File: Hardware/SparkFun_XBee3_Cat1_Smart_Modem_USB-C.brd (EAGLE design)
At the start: 53.3 x 59.7 mm, 112 parts, among them J1 USB Female Type C Connector, J3 USB Female Type C Connector, J4 QWIIC_RIGHT_ANGLE, U1 FSUSB30MUX_MSOP10, U2 AP63203, U3 ESD Diode, U5 ESD Diode, U6 CP210X

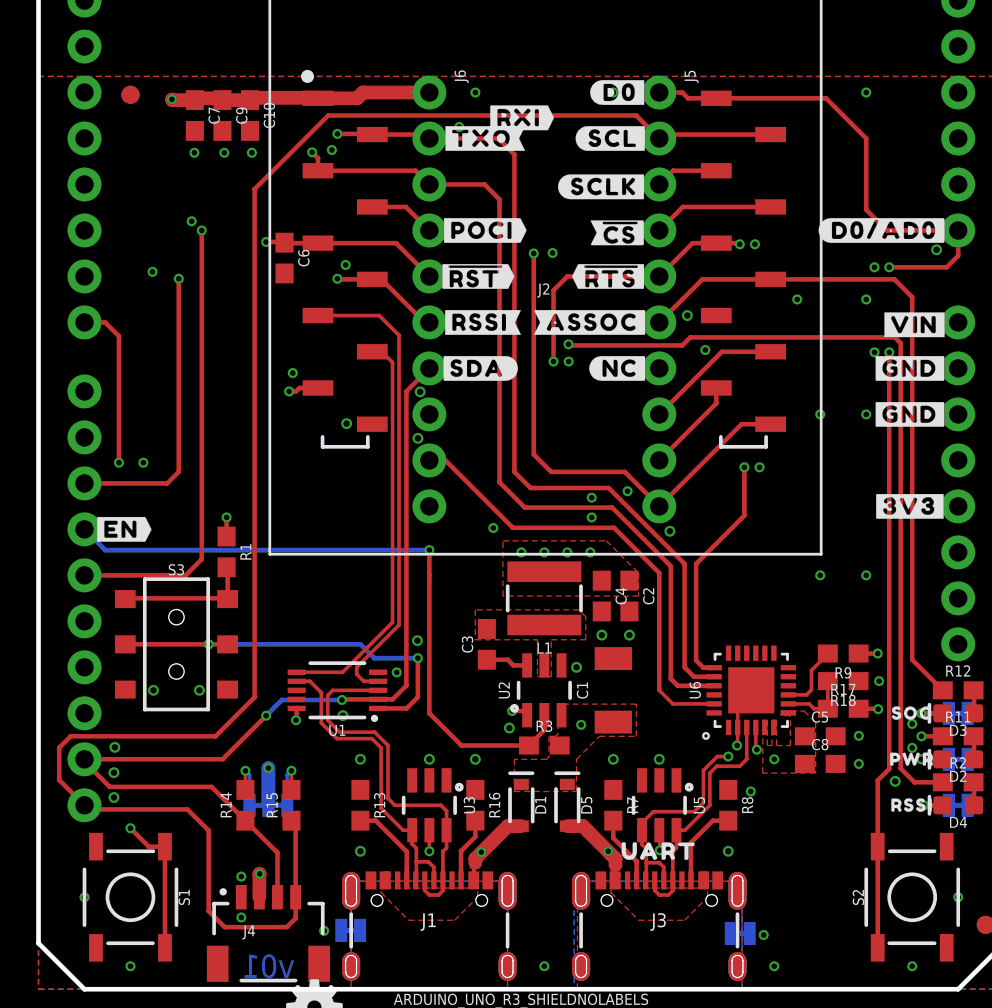
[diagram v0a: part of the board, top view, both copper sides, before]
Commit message: Updates many traces
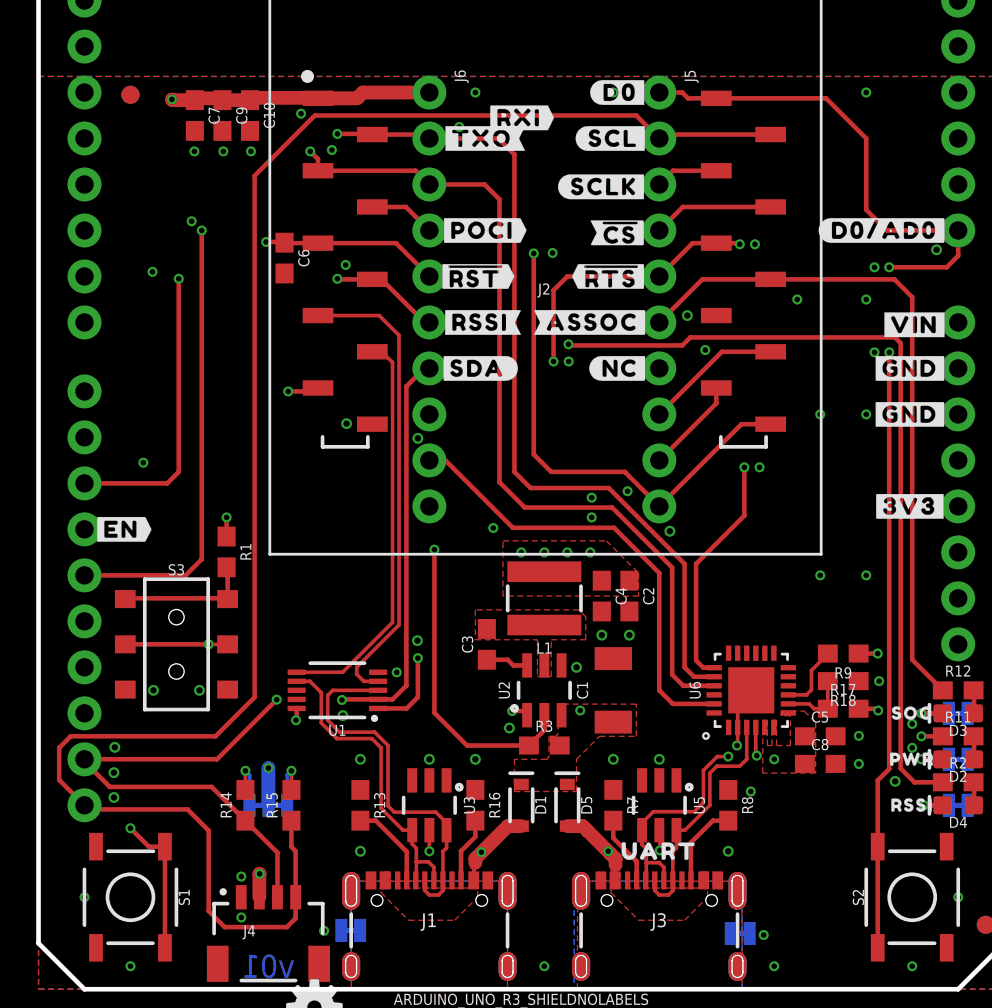
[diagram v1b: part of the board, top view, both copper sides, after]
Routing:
- net D7/!CTS!: track 49.5 -> 45.2 mm, vias 1 -> 0
- net D2/SPI_CLK: track 38.5 -> 37.3 mm
- net GND: vias 73 -> 72

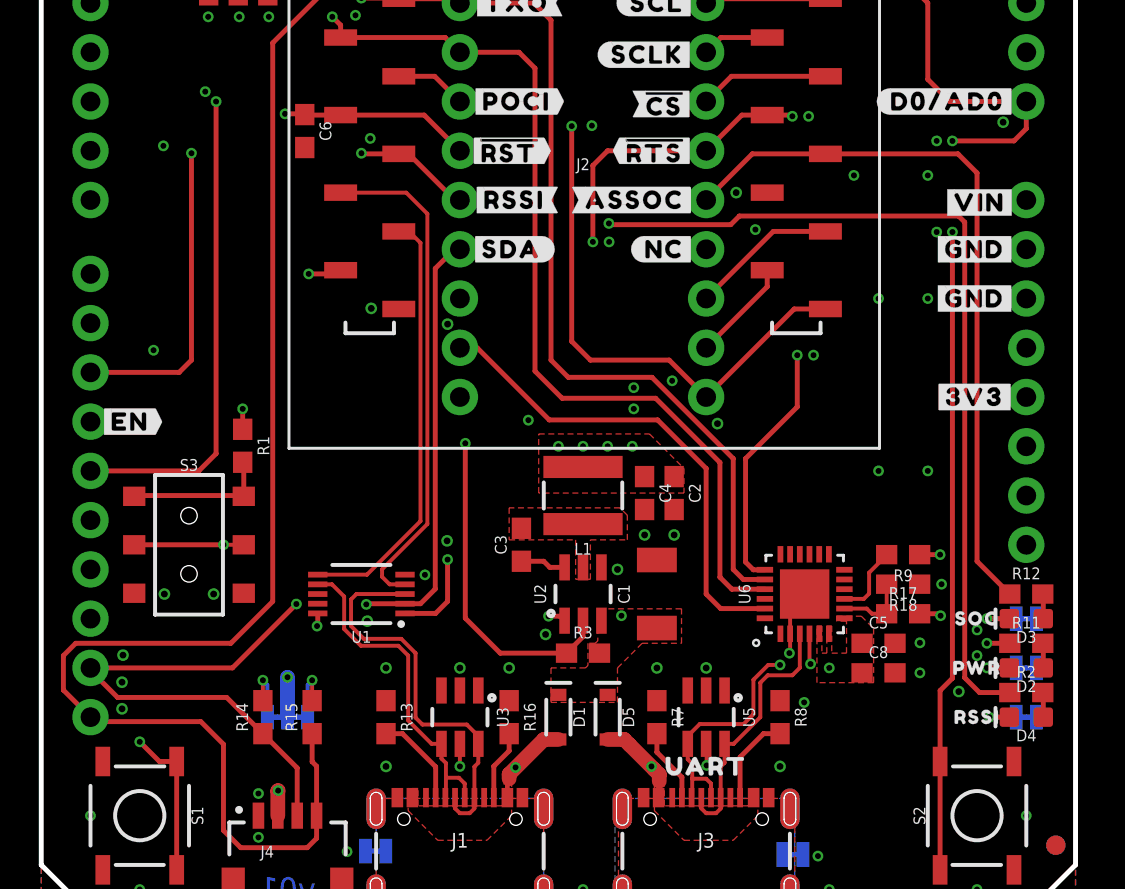
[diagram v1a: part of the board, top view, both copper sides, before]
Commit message: Makes all drill sizes uniform (0.012")
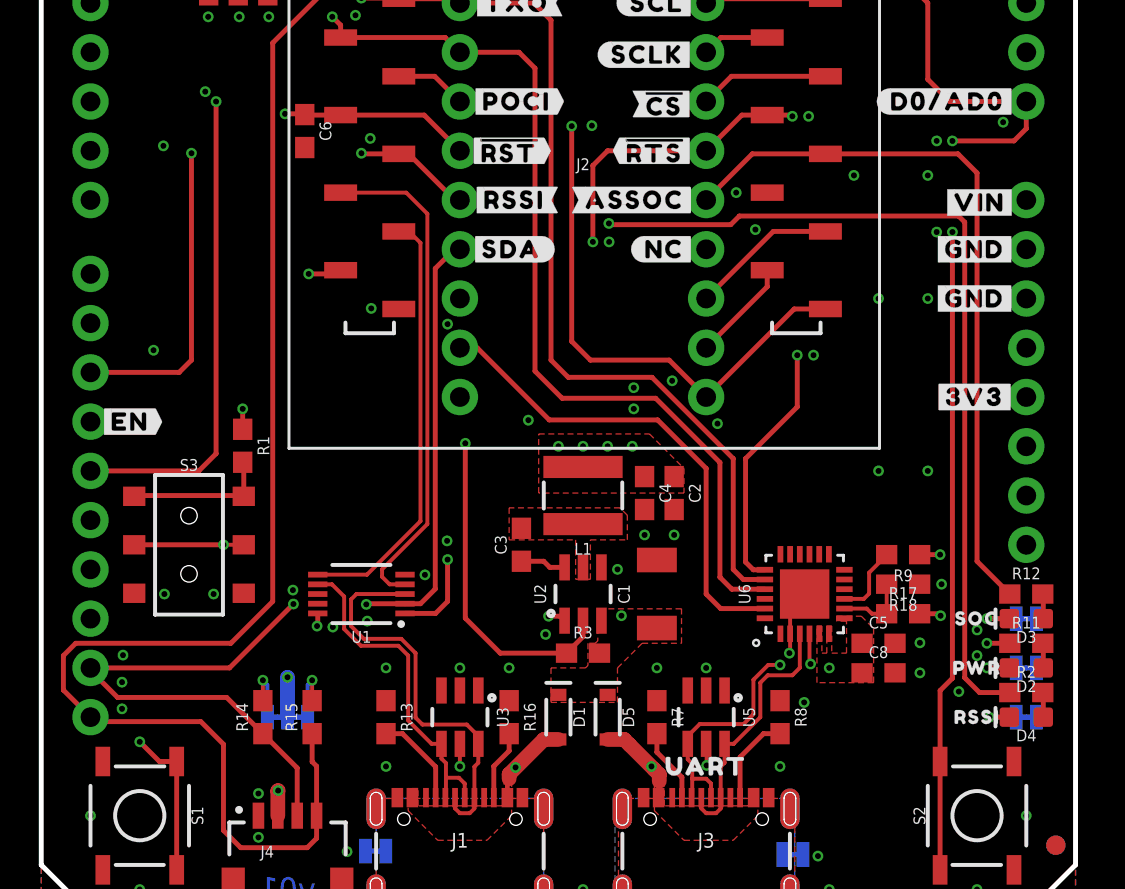
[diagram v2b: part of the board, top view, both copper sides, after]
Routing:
- net GND: vias 72 -> 74
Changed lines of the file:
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@@
 <wire x1="16.7974" y1="16.01" x2="16.764" y2="15.9766" width="0.254" layer="1"/>
 <via x="16.764" y="15.9766" extent="1-16" drill="0.3048"/>
-<wire x1="16.764" y1="15.9766" x2="13.1756" y2="15.9766" width="0.254" layer="2"/>
-<wire x1="13.1756" y1="15.9766" x2="13.1572" y2="15.995" width="0.254" layer="2"/>
-<via x="13.1572" y="15.995" extent="1-16" drill="0.3048"/>
+<wire x1="16.764" y1="15.9766" x2="13.0232" y2="15.9766" width="0.254" layer="2"/>
+<wire x1="13.0232" y1="15.9766" x2="13.0048" y2="15.995" width="0.254" layer="2"/>
+<via x="13.0048" y="15.995" extent="1-16" drill="0.3048"/>
 <wire x1="13.2" y1="5.08" x2="13.2" y2="7.54" width="0.254" layer="1"/>
 <wire x1="13.2" y1="7.54" x2="11.43" y2="9.31" width="0.254" layer="1"/>
@@
 <wire x1="3.937" y1="11.176" x2="2.54" y2="12.573" width="0.254" layer="1"/>
 <wire x1="2.54" y1="12.573" x2="2.54" y2="12.7" width="0.254" layer="1"/>
-<wire x1="2.54" y1="12.7" x2="9.8622" y2="12.7" width="0.254" layer="1"/>
-<wire x1="9.8622" y1="12.7" x2="13.1572" y2="15.995" width="0.254" layer="1"/>
+<wire x1="2.54" y1="12.7" x2="9.7098" y2="12.7" width="0.254" layer="1"/>
+<wire x1="9.7098" y1="12.7" x2="13.0048" y2="15.995" width="0.254" layer="1"/>
 <wire x1="20.32" y1="33.2994" x2="20.32" y2="16.77086875" width="0.254" layer="1"/>
 <wire x1="21.3106" y1="34.29" x2="20.32" y2="33.2994" width="0.254" layer="1"/>
@@
 <contactref element="RLED" pad="1"/>
 <contactref element="J6" pad="10"/>
-<via x="31.115" y="19.558" extent="1-16" drill="0.35"/>
-<via x="32.639" y="19.558" extent="1-16" drill="0.35"/>
-<via x="17.018" y="31.242" extent="1-16" drill="0.35"/>
+<via x="31.115" y="19.558" extent="1-16" drill="0.3048"/>
+<via x="32.639" y="19.558" extent="1-16" drill="0.3048"/>
+<via x="17.018" y="31.242" extent="1-16" drill="0.3048"/>
 <contactref element="J3" pad="GND"/>
 <contactref element="J3" pad="GND2"/>
@@
 <contactref element="C8" pad="2"/>
 <contactref element="C5" pad="2"/>
-<via x="29.718" y="17.78" extent="1-16" drill="0.35"/>
+<via x="29.718" y="17.78" extent="1-16" drill="0.3048"/>
 <wire x1="38.62" y1="14.46" x2="38.62" y2="15.76" width="0.2032" layer="1"/>
 <wire x1="38.62" y1="15.76" x2="39.37" y2="16.51" width="0.2032" layer="1"/>
@@
 <via x="25.1206" y="25.4762" extent="1-16" drill="0.3048"/>
 <via x="32.5374" y="27.5082" extent="1-16" drill="0.3048"/>
-<via x="26.0096" y="14.4272" extent="1-16" drill="0.35"/>
-<via x="20.9296" y="19.2532" extent="1-16" drill="0.35"/>
-<via x="16.8148" y="15.113" extent="1-16" drill="0.35"/>
-<via x="20.955" y="30.4292" extent="1-16" drill="0.35"/>
-<via x="34.8742" y="25.2984" extent="1-16" drill="0.35"/>
-<via x="35.8394" y="37.211" extent="1-16" drill="0.35"/>
-<via x="49.6062" y="40.8432" extent="1-16" drill="0.35"/>
-<via x="47.3202" y="11.4808" extent="1-16" drill="0.35"/>
-<via x="31.75" y="12.7" extent="1-16" drill="0.35"/>
-<via x="24.13" y="12.7" extent="1-16" drill="0.35"/>
-<via x="21.59" y="12.7" extent="1-16" drill="0.35"/>
-<via x="34.29" y="12.7" extent="1-16" drill="0.35"/>
-<via x="17.78" y="12.7" extent="1-16" drill="0.35"/>
-<via x="4.1656" y="11.9634" extent="1-16" drill="0.35"/>
-<via x="4.2164" y="13.3604" extent="1-16" drill="0.35"/>
+<via x="26.0096" y="14.4272" extent="1-16" drill="0.3048"/>
+<via x="20.9296" y="19.2532" extent="1-16" drill="0.3048"/>
+<via x="16.8148" y="15.113" extent="1-16" drill="0.3048"/>
+<via x="20.955" y="30.4292" extent="1-16" drill="0.3048"/>
+<via x="34.8742" y="25.2984" extent="1-16" drill="0.3048"/>
+<via x="35.8394" y="37.211" extent="1-16" drill="0.3048"/>
+<via x="49.6062" y="40.8432" extent="1-16" drill="0.3048"/>
+<via x="47.3202" y="11.4808" extent="1-16" drill="0.3048"/>
+<via x="31.75" y="12.7" extent="1-16" drill="0.3048"/>
+<via x="24.13" y="12.7" extent="1-16" drill="0.3048"/>
+<via x="21.59" y="12.7" extent="1-16" drill="0.3048"/>
+<via x="34.29" y="12.7" extent="1-16" drill="0.3048"/>
+<via x="17.78" y="12.7" extent="1-16" drill="0.3048"/>
+<via x="4.1656" y="11.9634" extent="1-16" drill="0.3048"/>
+<via x="4.2164" y="13.3604" extent="1-16" drill="0.3048"/>
 <via x="2.54" y="5.08" extent="1-16" drill="0.3048"/>
-<via x="8.89" y="16.51" extent="1-16" drill="0.35"/>
-<via x="6.35" y="16.51" extent="1-16" drill="0.35"/>
-<via x="17.78" y="7.62" extent="1-16" drill="0.35"/>
-<via x="38.1" y="7.62" extent="1-16" drill="0.35"/>
-<via x="4.1656" y="10.5918" extent="1-16" drill="0.35"/>
+<via x="8.89" y="16.51" extent="1-16" drill="0.3048"/>
+<via x="6.35" y="16.51" extent="1-16" drill="0.3048"/>
+<via x="17.78" y="7.62" extent="1-16" drill="0.3048"/>
+<via x="38.1" y="7.62" extent="1-16" drill="0.3048"/>
+<via x="4.1656" y="10.5918" extent="1-16" drill="0.3048"/>
 <via x="50.8" y="5.08" extent="1-16" drill="0.3048"/>
 <via x="48.26" y="14.6558" extent="1-16" drill="0.3048"/>
 <via x="48.26" y="13.335" extent="1-16" drill="0.3048"/>
 <via x="14.5034" y="48.3616" extent="1-16" drill="0.3048"/>
+<via x="15.0368" y="14.8082" extent="1-16" drill="0.3048"/>
+<via x="12.9794" y="16.7132" extent="1-16" drill="0.3048"/>
 </signal>
 <signal name="3.3V">

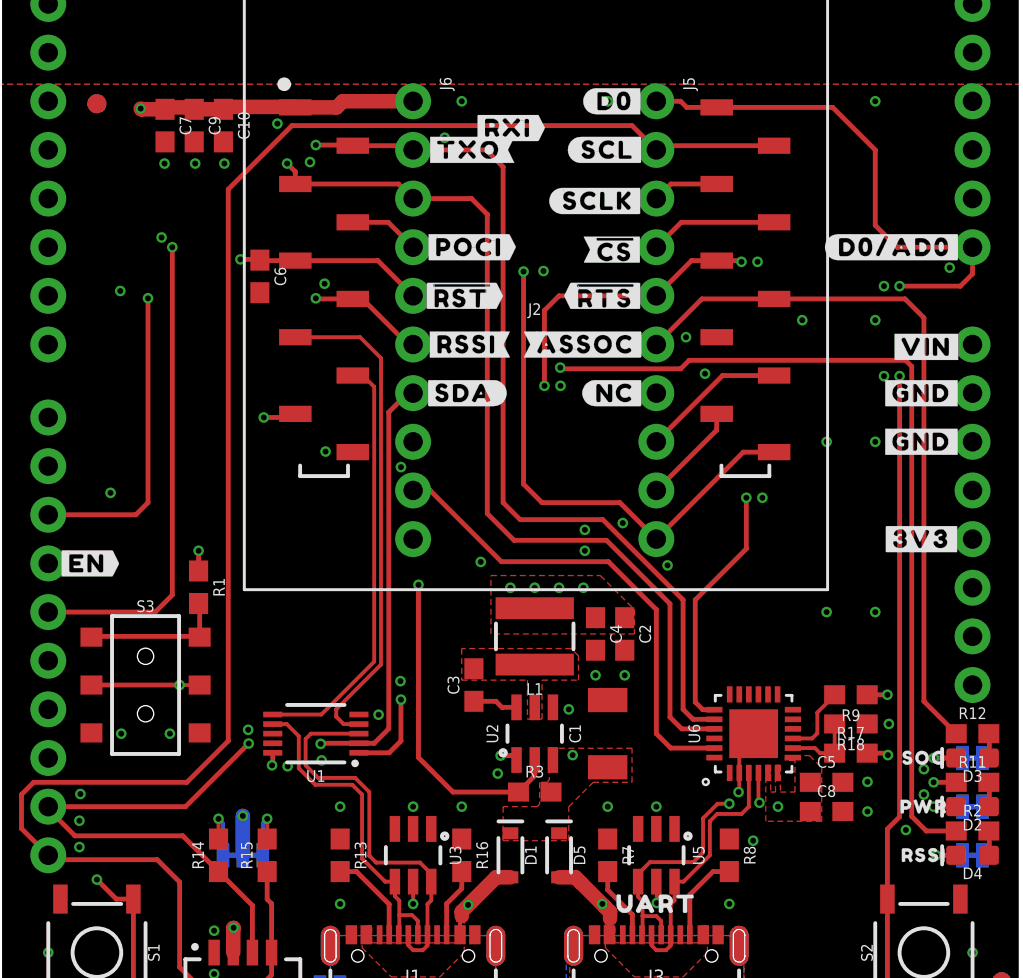
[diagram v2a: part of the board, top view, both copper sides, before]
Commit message: Adds some silk
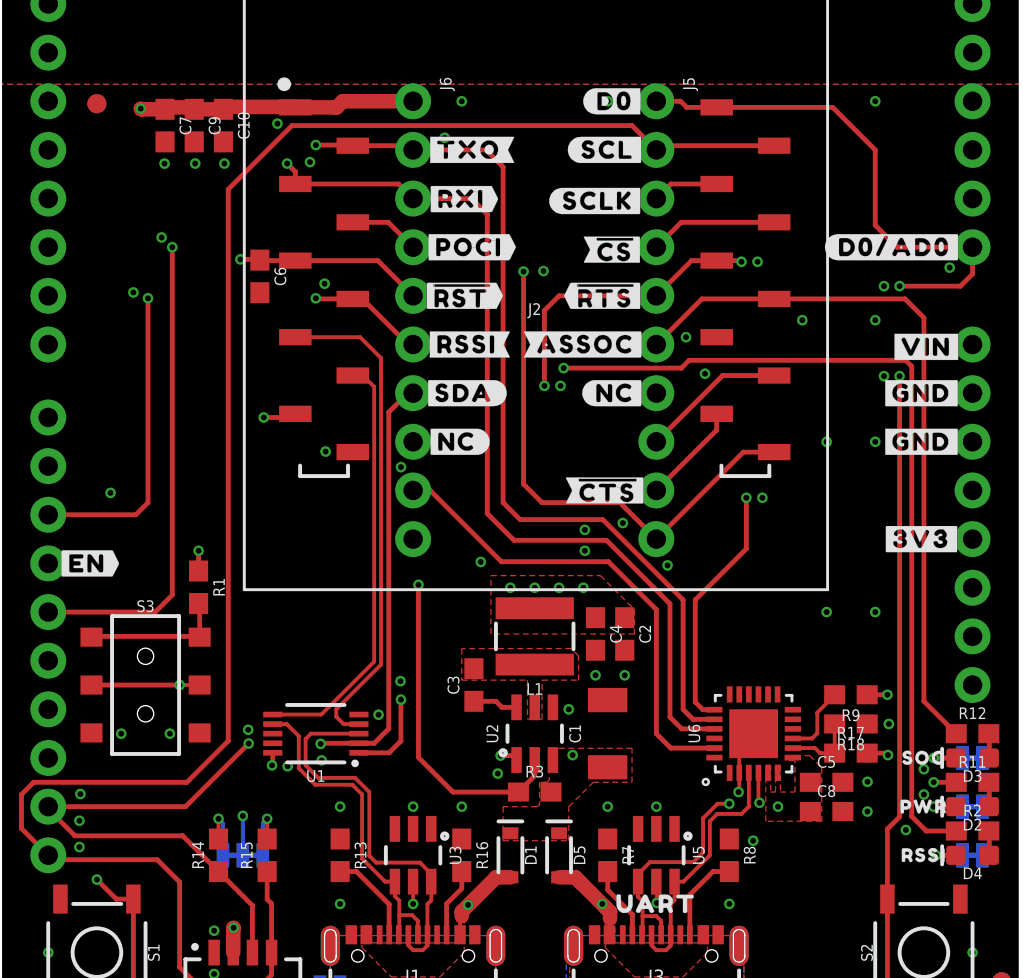
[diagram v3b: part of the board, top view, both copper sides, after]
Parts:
- added U$31: (no value), topmirror:##CTS##26
- added U$9: (no value), topmirror:#NC#1
- moved U$27 4.44 mm to (24.1, 44.4)
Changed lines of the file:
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@@
 <layer number="19" name="Unrouted" color="6" fill="1" visible="yes" active="yes"/>
 <layer number="20" name="Dimension" color="15" fill="1" visible="yes" active="yes"/>
-<layer number="21" name="tPlace" color="16" fill="1" visible="no" active="yes"/>
-<layer number="22" name="bPlace" color="14" fill="1" visible="no" active="yes"/>
+<layer number="21" name="tPlace" color="16" fill="1" visible="yes" active="yes"/>
+<layer number="22" name="bPlace" color="14" fill="1" visible="yes" active="yes"/>
 <layer number="23" name="tOrigins" color="15" fill="1" visible="yes" active="yes"/>
 <layer number="24" name="bOrigins" color="15" fill="1" visible="yes" active="yes"/>
@@
 <layer number="37" name="tTest" color="7" fill="1" visible="no" active="yes"/>
 <layer number="38" name="bTest" color="7" fill="1" visible="no" active="yes"/>
-<layer number="39" name="tKeepout" color="4" fill="11" visible="yes" active="yes"/>
+<layer number="39" name="tKeepout" color="4" fill="11" visible="no" active="yes"/>
 <layer number="40" name="bKeepout" color="1" fill="11" visible="no" active="yes"/>
 <layer number="41" name="tRestrict" color="4" fill="10" visible="no" active="yes"/>
@@
 <element name="U$52" library="topmirror" package="#PLED#20" value="" x="64.008" y="31.369" smashed="yes" rot="MR0"/>
 <element name="U$21" library="botmirror" package="#TXO#8" value="" x="24.511" y="46.99" smashed="yes"/>
-<element name="U$27" library="botmirror" package="#RXI#7" value="" x="26.543" y="48.133" smashed="yes"/>
+<element name="U$27" library="botmirror" package="#RXI#7" value="" x="24.1046" y="44.4246" smashed="yes"/>
 <element name="U$45" library="botmirror" package="#POCI#32" value="" x="24.511" y="41.91" smashed="yes"/>
 <element name="U$54" library="botmirror" package="##RST##13" value="" x="24.13" y="39.37" smashed="yes"/>
@@
 </element>
 <element name="U$29" library="topmirror" package="#GND#0" value="" x="48.133" y="34.29" smashed="yes"/>
+<element name="U$9" library="topmirror" package="#NC#1" value="" x="23.876" y="31.75" smashed="yes"/>
+<element name="U$31" library="topmirror" package="##CTS##26" value="" x="31.75" y="29.21" smashed="yes"/>
 </elements>
 <signals>
@@
 <via x="16.9672" y="40.005" extent="1-16" drill="0.3048"/>
 <via x="8.4582" y="42.418" extent="1-16" drill="0.3048"/>
-<via x="6.2992" y="39.624" extent="1-16" drill="0.3048"/>
+<via x="6.985" y="39.5478" extent="1-16" drill="0.3048"/>
 <via x="45.72" y="31.75" extent="1-16" drill="0.3048"/>
 <via x="45.72" y="38.1" extent="1-16" drill="0.3048"/>
@@
 <wire x1="8.636" y1="49.11" x2="8.736" y2="49.21" width="0.762" layer="1"/>
 <via x="27.94" y="24.13" extent="1-16" drill="0.3048"/>
-<wire x1="12.7" y1="10.16" x2="12.7" y2="12.2174" width="0.762" layer="16"/>
 <via x="40.64" y="12.7" extent="1-16" drill="0.3048"/>
 <polygon width="0.254" layer="15" isolate="0.127" rank="3">
@@
 <wire x1="12.2" y1="6.358" x2="12.2174" y2="6.3754" width="0.762" layer="1"/>
 <via x="12.2174" y="6.3754" extent="1-16" drill="0.3048"/>
+<wire x1="12.7" y1="10.16" x2="12.7" y2="12.2174" width="0.2032" layer="16"/>
 </signal>
 <signal name="N$11">
@@
 <wire x1="47.625" y1="12.192" x2="47.625" y2="35.687" width="0.254" layer="1"/>
 <wire x1="47.625" y1="35.687" x2="47.3075" y2="36.0045" width="0.254" layer="1"/>
-<wire x1="29.21" y1="35.56" x2="29.2735" y2="35.6235" width="0.254" layer="1"/>
-<via x="29.2735" y="35.6235" extent="1-16" drill="0.3048"/>
-<wire x1="29.2735" y1="35.6235" x2="23.8125" y2="35.6235" width="0.254" layer="2"/>
-<wire x1="23.8125" y1="35.6235" x2="22.606" y2="36.83" width="0.254" layer="2"/>
+<via x="29.4513" y="35.5981" extent="1-16" drill="0.3048"/>
+<wire x1="29.4513" y1="35.5981" x2="23.8379" y2="35.5981" width="0.254" layer="2"/>
+<wire x1="23.8379" y1="35.5981" x2="22.606" y2="36.83" width="0.254" layer="2"/>
 <wire x1="22.606" y1="36.83" x2="21.59" y2="36.83" width="0.254" layer="2"/>
-<wire x1="47.3075" y1="36.0045" x2="36.0045" y2="36.0045" width="0.254" layer="1"/>
-<wire x1="29.21" y1="35.56" x2="35.56" y2="35.56" width="0.254" layer="1"/>
-<wire x1="35.56" y1="35.56" x2="36.0045" y2="36.0045" width="0.254" layer="1"/>
+<wire x1="36.0045" y1="36.0045" x2="47.3075" y2="36.0045" width="0.254" layer="1"/>
 <wire x1="7.747" y1="39.243" x2="7.747" y2="28.575" width="0.254" layer="1"/>
 <via x="7.747" y="39.243" extent="1-16" drill="0.3048"/>
@@
 <wire x1="2.54" y1="27.94" x2="7.112" y2="27.94" width="0.254" layer="1"/>
 <wire x1="18.948" y1="39.21" x2="18.44" y2="39.21" width="0.254" layer="1"/>
+<wire x1="29.4513" y1="35.5981" x2="35.5981" y2="35.5981" width="0.254" layer="1"/>
+<wire x1="35.5981" y1="35.5981" x2="36.0045" y2="36.0045" width="0.254" layer="1"/>
 </signal>
 <signal name="D8/!DTR!">
